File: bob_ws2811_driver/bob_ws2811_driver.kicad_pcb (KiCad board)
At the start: 2 copper layers, 100 x 50 mm, 40 parts

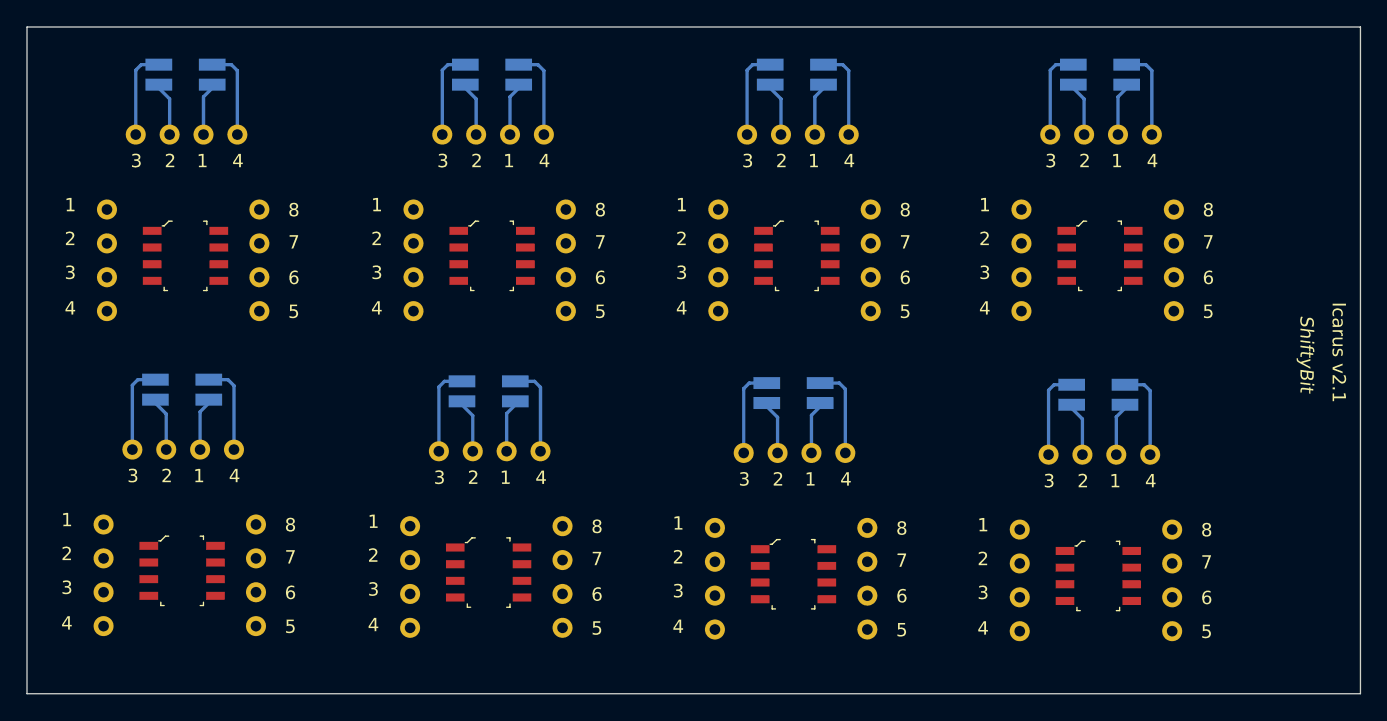
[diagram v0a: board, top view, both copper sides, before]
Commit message: Fixed Icarus. Actually routed the tracks for the ws2811 dip adapter
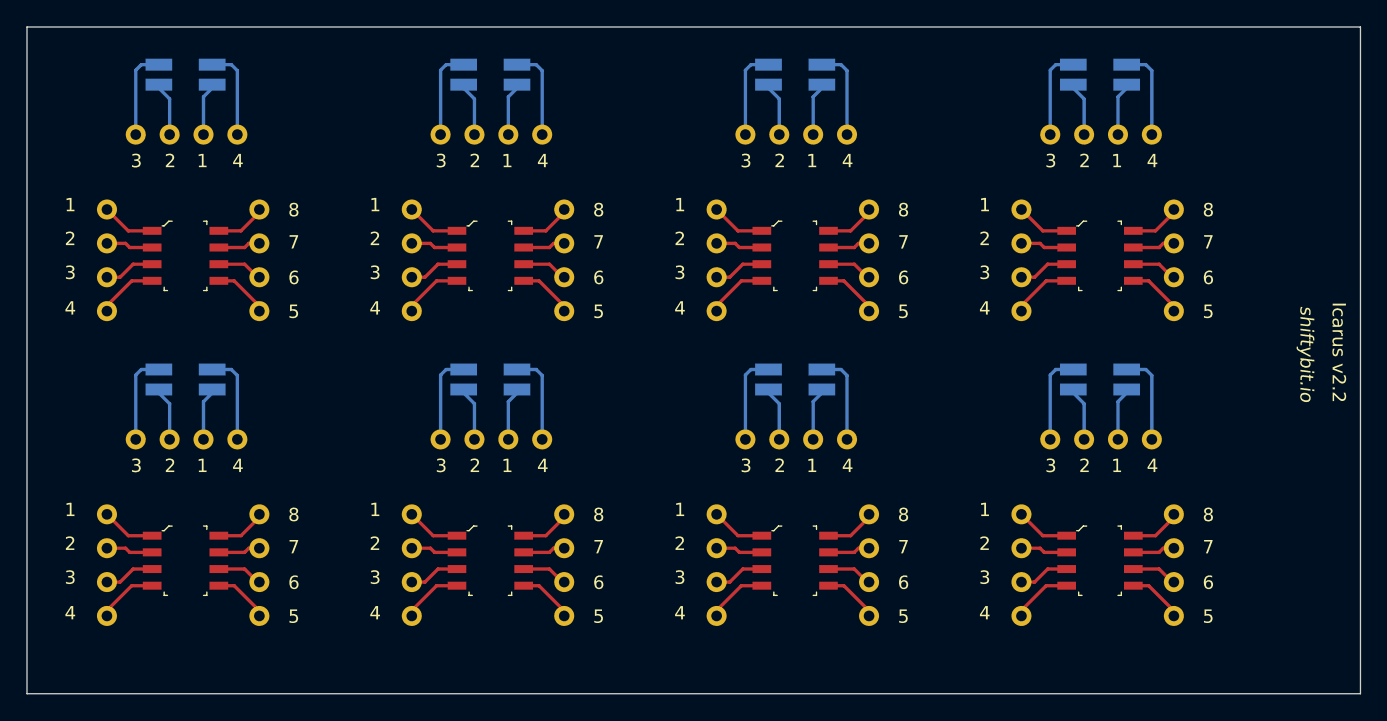
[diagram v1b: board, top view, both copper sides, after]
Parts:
- removed the REF** at (157.5, 52.5)
- removed the REF** at (140.5, 42.4)
- removed the REF** at (129.0, 42.4)
- removed the REF** at (163.3, 42.4)
- removed the REF** at (151.9, 42.4)
- removed the REF** at (157.7, 28.6)
- removed the REF** at (157.7, 42.2)
- removed the REF** at (157.7, 33.0)
- removed the REF** at (134.9, 28.6)
- removed the REF** at (180.3, 66.2)
- removed the REF** at (180.3, 57.0)
- removed the REF** at (174.5, 66.4)
- removed the REF** at (180.3, 52.6)
- removed the REF** at (185.9, 66.4)
- removed the REF** at (157.5, 66.0)
- removed the REF** at (163.1, 66.3)
- removed the REF** at (151.6, 66.3)
- removed the REF** at (157.5, 56.9)
- removed the REF** at (140.2, 66.2)
- removed the REF** at (128.8, 66.2)
- removed the REF** at (134.6, 56.8)
- removed the REF** at (134.6, 52.3)
- removed the REF** at (134.6, 65.9)
- removed the REF** at (117.2, 66.0)
- removed the REF** at (105.8, 66.0)
- removed the REF** at (111.6, 56.6)
- removed the REF** at (111.6, 52.2)
- removed the REF** at (111.6, 65.8)
- removed the REF** at (134.9, 33.0)
- removed the REF** at (134.9, 42.2)
- added REF**: VAL**, ShiftyBit:SunLed, B.Cu at (111.9, 51.4)
- added REF**: 4x1_ProtoBoard, TEST2:4x1_ProtoBoard, F.Cu at (128.9, 65.3)
- added REF**: 4x1_ProtoBoard, TEST2:4x1_ProtoBoard, F.Cu at (157.6, 55.9)
- added REF**: VAL**, ShiftyBit:SunLed, B.Cu at (157.6, 51.4)
- added REF**: WS2811-Driver-Chip, ShiftyBit:WS2811-Driver-Chip, F.Cu at (157.6, 65.0)
- added REF**: 4x1_ProtoBoard, TEST2:4x1_ProtoBoard, F.Cu at (163.2, 65.3)
- added REF**: 4x1_ProtoBoard, TEST2:4x1_ProtoBoard, F.Cu at (151.8, 65.3)
- added REF**: 4x1_ProtoBoard, TEST2:4x1_ProtoBoard, F.Cu at (186.1, 65.3)
- added REF**: 4x1_ProtoBoard, TEST2:4x1_ProtoBoard, F.Cu at (174.6, 65.3)
- added REF**: 4x1_ProtoBoard, TEST2:4x1_ProtoBoard, F.Cu at (180.5, 55.9)
- added REF**: VAL**, ShiftyBit:SunLed, B.Cu at (180.5, 51.4)
- added REF**: WS2811-Driver-Chip, ShiftyBit:WS2811-Driver-Chip, F.Cu at (111.9, 65.0)
- added REF**: WS2811-Driver-Chip, ShiftyBit:WS2811-Driver-Chip, F.Cu at (180.5, 65.0)
- added REF**: 4x1_ProtoBoard, TEST2:4x1_ProtoBoard, F.Cu at (151.8, 42.4)
- added REF**: 4x1_ProtoBoard, TEST2:4x1_ProtoBoard, F.Cu at (163.2, 42.4)
- added REF**: WS2811-Driver-Chip, ShiftyBit:WS2811-Driver-Chip, F.Cu at (157.6, 42.2)
- added REF**: 4x1_ProtoBoard, TEST2:4x1_ProtoBoard, F.Cu at (157.6, 33.0)
- added REF**: 4x1_ProtoBoard, TEST2:4x1_ProtoBoard, F.Cu at (111.9, 55.9)
- added REF**: VAL**, ShiftyBit:SunLed, B.Cu at (157.6, 28.6)
- added REF**: VAL**, ShiftyBit:SunLed, B.Cu at (134.7, 28.6)
- added REF**: 4x1_ProtoBoard, TEST2:4x1_ProtoBoard, F.Cu at (128.9, 42.4)
- added REF**: 4x1_ProtoBoard, TEST2:4x1_ProtoBoard, F.Cu at (134.7, 33.0)
- added REF**: 4x1_ProtoBoard, TEST2:4x1_ProtoBoard, F.Cu at (140.3, 42.4)
- added REF**: WS2811-Driver-Chip, ShiftyBit:WS2811-Driver-Chip, F.Cu at (134.7, 42.2)
- added REF**: 4x1_ProtoBoard, TEST2:4x1_ProtoBoard, F.Cu at (117.5, 65.3)
- added REF**: 4x1_ProtoBoard, TEST2:4x1_ProtoBoard, F.Cu at (106.0, 65.3)
- added REF**: 4x1_ProtoBoard, TEST2:4x1_ProtoBoard, F.Cu at (134.7, 55.9)
- added REF**: VAL**, ShiftyBit:SunLed, B.Cu at (134.7, 51.4)
- added REF**: WS2811-Driver-Chip, ShiftyBit:WS2811-Driver-Chip, F.Cu at (134.7, 65.0)
- added REF**: 4x1_ProtoBoard, TEST2:4x1_ProtoBoard, F.Cu at (140.3, 65.3)
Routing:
- net (no net): track 171.1 -> 415.8 mm
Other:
- board text added: "Icarus v2.2"
- board text added: "shiftybit.io"
- board text removed: "Icarus v2.1"
- board text removed: "ShiftyBit"
